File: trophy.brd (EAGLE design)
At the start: 75.9 x 26.7 mm, 20 parts, among them J1 AVR_SPI_PROG_3X2PTH, U1 ATTINY85SOIC8

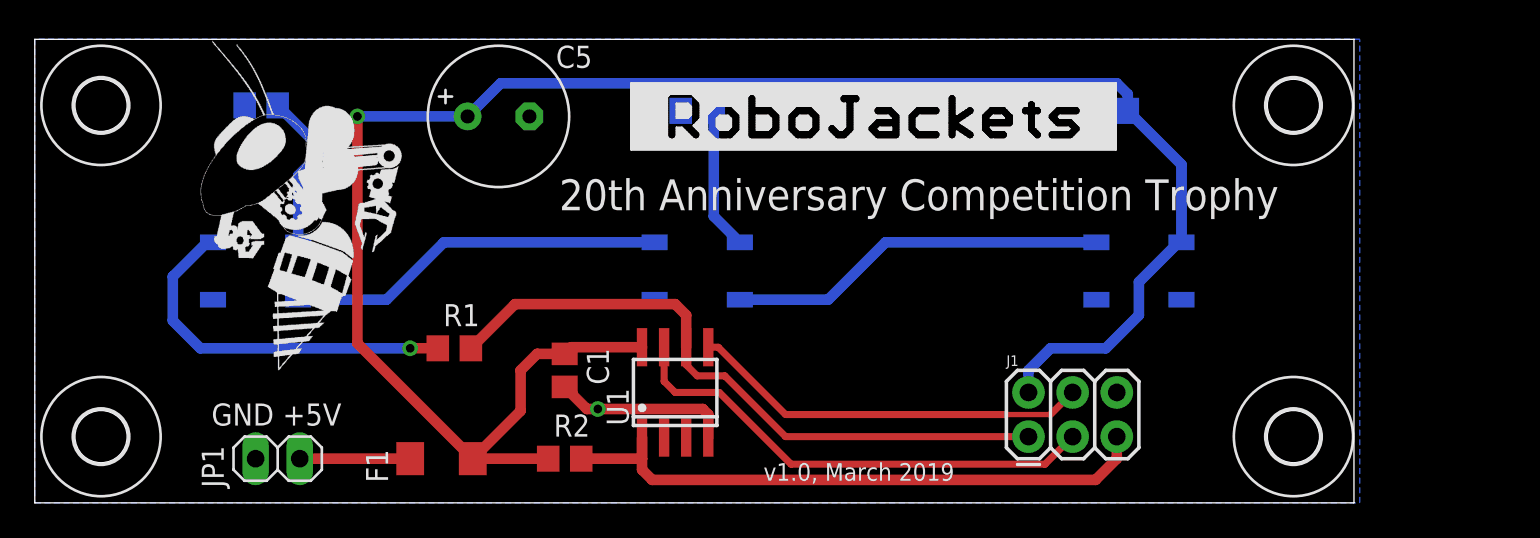
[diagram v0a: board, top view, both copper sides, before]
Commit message: Round corners and make final tweaks for trophy
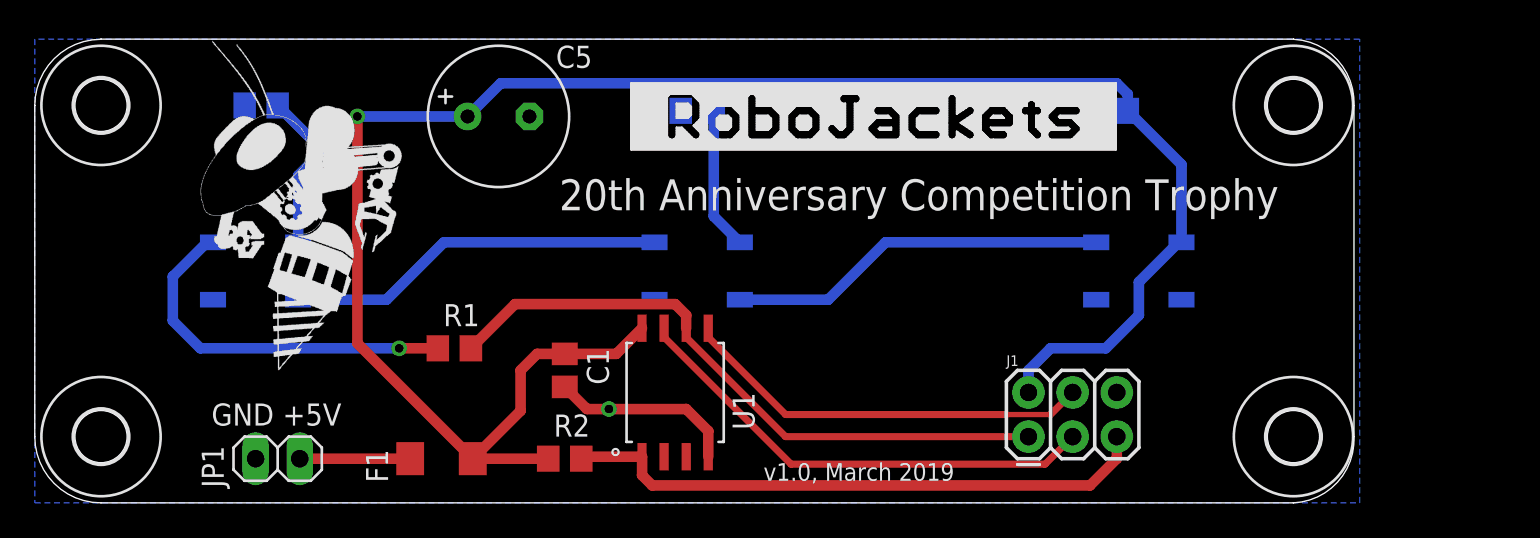
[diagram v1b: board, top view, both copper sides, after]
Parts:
- U1: value ATTINY85SOIC8 -> ATTINY85; device JoshCustom:SOIC8 -> JoshCustom:8S2
- turned U1 to 90 degrees
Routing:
- net MISO: track 38.0 -> 37.0 mm
- net MOSI: track 23.1 -> 23.8 mm
- net !RESET!: track 34.7 -> 34.1 mm
- net GND: track 10.2 -> 10.8 mm
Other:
- outline, holes or cut-outs redrawn
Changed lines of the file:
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@@
 <layer number="49" name="Reference" color="7" fill="1" visible="yes" active="yes"/>
 <layer number="50" name="dxf" color="7" fill="1" visible="no" active="no"/>
-<layer number="51" name="tDocu" color="7" fill="1" visible="yes" active="yes"/>
-<layer number="52" name="bDocu" color="7" fill="1" visible="yes" active="yes"/>
+<layer number="51" name="tDocu" color="7" fill="1" visible="no" active="yes"/>
+<layer number="52" name="bDocu" color="7" fill="1" visible="no" active="yes"/>
 <layer number="53" name="tGND_GNDA" color="7" fill="9" visible="no" active="no"/>
 <layer number="54" name="bGND_GNDA" color="1" fill="9" visible="no" active="no"/>
@@
 <board>
 <plain>
-<wire x1="0" y1="0" x2="75.87" y2="0" width="0" layer="20"/>
-<wire x1="75.87" y1="0" x2="75.87" y2="26.66" width="0" layer="20"/>
-<wire x1="75.87" y1="26.66" x2="0" y2="26.66" width="0" layer="20"/>
-<wire x1="0" y1="26.66" x2="0" y2="0" width="0" layer="20"/>
+<wire x1="3.81" y1="0" x2="72.39" y2="0" width="0" layer="20"/>
+<wire x1="72.39" y1="0" x2="75.87" y2="3.81" width="0" layer="20" curve="90"/>
+<wire x1="75.87" y1="3.81" x2="75.87" y2="22.85" width="0" layer="20"/>
+<wire x1="75.87" y1="22.85" x2="72.4" y2="26.66" width="0" layer="20" curve="90"/>
+<wire x1="72.4" y1="26.66" x2="72.39" y2="26.67" width="0" layer="20"/>
+<wire x1="72.39" y1="26.67" x2="3.81" y2="26.67" width="0" layer="20"/>
+<wire x1="3.81" y1="26.67" x2="3.8" y2="26.66" width="0" layer="20"/>
+<wire x1="3.8" y1="26.66" x2="0" y2="22.85" width="0" layer="20" curve="90"/>
+<wire x1="0" y1="22.85" x2="0" y2="22.86" width="0" layer="20"/>
+<wire x1="0" y1="22.85" x2="0" y2="3.81" width="0" layer="20"/>
+<wire x1="0" y1="3.81" x2="3.81" y2="0" width="0" layer="20" curve="90"/>
 <text x="10.16" y="4.445" size="1.27" layer="21">GND +5V</text>
-<text x="30.1625" y="16.8275" size="1.778" layer="21">20th Anniversary Competition Trophy</text>
-<text x="41.91" y="1.27" size="1.016" layer="21">v1.0, March 2019</text>
+<text x="30.1625" y="16.8275" size="1.778" layer="21" font="vector">20th Anniversary Competition Trophy</text>
+<text x="41.91" y="1.27" size="1.016" layer="21" font="vector" ratio="7">v1.0, March 2019</text>
 </plain>
 <attributes>
@@
 <attribute name="NAME" x="29.845" y="3.81" size="1.27" layer="25" ratio="7"/>
 </element>
-<element name="U1" library="JoshCustom" package="SOIC8" value="ATTINY85SOIC8" x="36.83" y="6.35" smashed="yes">
-<attribute name="NAME" x="34.163" y="4.445" size="1.27" layer="25" font="vector" ratio="7" rot="R90"/>
+<element name="U1" library="JoshCustom" package="8S2" value="ATTINY85" x="36.83" y="6.35" smashed="yes" rot="R90">
+<attribute name="NAME" x="40.132" y="6.35" size="1.27" layer="25" font="vector" ratio="7" rot="R270"/>
 </element>
 <element name="U$1" library="holes" library_urn="urn:adsk.eagle:library:237" package="3,0" package3d_urn="urn:adsk.eagle:package:14277/1" value="" x="3.81" y="3.81" smashed="yes"/>
@@
 <wire x1="27.94" y1="7.62" x2="28.89" y2="8.57" width="0.6096" layer="1"/>
 <wire x1="28.89" y1="8.57" x2="30.48" y2="8.57" width="0.6096" layer="1"/>
-<wire x1="30.48" y1="8.57" x2="30.86" y2="8.95" width="0.6096" layer="1"/>
-<wire x1="30.86" y1="8.95" x2="34.925" y2="8.95" width="0.6096" layer="1"/>
 <wire x1="24.892" y1="22.225" x2="18.555" y2="22.225" width="0.6096" layer="16"/>
 <wire x1="18.555" y1="22.225" x2="16.57875" y2="20.24875" width="0.6096" layer="16"/>
@@
 <wire x1="63.5" y1="12.7" x2="65.785" y2="14.985" width="0.6096" layer="16"/>
 <wire x1="65.785" y1="14.985" x2="65.95" y2="14.985" width="0.6096" layer="16"/>
+<wire x1="30.48" y1="8.57" x2="33.4493" y2="8.57" width="0.6096" layer="1"/>
+<wire x1="34.925" y1="10.0457" x2="33.4493" y2="8.57" width="0.6096" layer="1"/>
 </signal>
 <signal name="GND">
@@
 </polygon>
 <wire x1="30.48" y1="6.67" x2="31.7525" y2="5.3975" width="0.6096" layer="1"/>
-<wire x1="38.4175" y1="5.3975" x2="38.735" y2="5.08" width="0.6096" layer="1"/>
-<wire x1="38.735" y1="5.08" x2="38.735" y2="3.75" width="0.6096" layer="1"/>
-<wire x1="31.7525" y1="5.3975" x2="32.385" y2="5.3975" width="0.6096" layer="1"/>
-<wire x1="32.385" y1="5.3975" x2="38.4175" y2="5.3975" width="0.6096" layer="1"/>
-<via x="32.385" y="5.3975" extent="1-16" drill="0.5"/>
+<wire x1="31.7525" y1="5.3975" x2="33.02" y2="5.3975" width="0.6096" layer="1"/>
+<via x="33.02" y="5.3975" extent="1-16" drill="0.5"/>
+<wire x1="37.465" y1="5.3975" x2="38.735" y2="4.1275" width="0.6096" layer="1"/>
+<wire x1="37.465" y1="5.3975" x2="33.02" y2="5.3975" width="0.6096" layer="1"/>
+<wire x1="38.735" y1="4.1275" x2="38.735" y2="2.6543" width="0.6096" layer="1"/>
 </signal>
 <signal name="N$1">
@@
 <contactref element="R2" pad="2"/>
 <contactref element="J1" pad="5"/>
-<wire x1="34.925" y1="3.75" x2="34.925" y2="2.54" width="0.6096" layer="1"/>
-<wire x1="34.925" y1="2.54" x2="34.925" y2="1.905" width="0.6096" layer="1"/>
-<wire x1="34.925" y1="1.905" x2="35.5092" y2="1.3208" width="0.6096" layer="1"/>
-<wire x1="61.0108" y1="1.3208" x2="62.23" y2="2.54" width="0.6096" layer="1"/>
+<wire x1="35.5092" y1="1.0033" x2="34.925" y2="1.5875" width="0.6096" layer="1"/>
+<wire x1="60.6933" y1="1.0033" x2="62.23" y2="2.54" width="0.6096" layer="1"/>
 <wire x1="62.23" y1="2.54" x2="62.23" y2="3.81" width="0.6096" layer="1"/>
-<wire x1="35.5092" y1="1.3208" x2="61.0108" y2="1.3208" width="0.6096" layer="1"/>
-<wire x1="31.43" y1="2.54" x2="34.925" y2="2.54" width="0.6096" layer="1"/>
+<wire x1="35.5092" y1="1.0033" x2="60.6933" y2="1.0033" width="0.6096" layer="1"/>
+<wire x1="31.43" y1="2.54" x2="31.5443" y2="2.6543" width="0.6096" layer="1"/>
+<wire x1="31.5443" y1="2.6543" x2="34.925" y2="2.6543" width="0.6096" layer="1"/>
+<wire x1="34.925" y1="1.5875" x2="34.925" y2="2.6543" width="0.6096" layer="1"/>
 </signal>
 <signal name="SCK">
 <contactref element="U1" pad="7"/>
 <contactref element="J1" pad="3"/>
-<wire x1="36.195" y1="8.95" x2="36.195" y2="6.985" width="0.4064" layer="1"/>
-<wire x1="36.195" y1="6.985" x2="36.83" y2="6.35" width="0.4064" layer="1"/>
-<wire x1="36.83" y1="6.35" x2="39.37" y2="6.35" width="0.4064" layer="1"/>
-<wire x1="39.37" y1="6.35" x2="43.4975" y2="2.2225" width="0.4064" layer="1"/>
-<wire x1="43.4975" y1="2.2225" x2="58.1025" y2="2.2225" width="0.4064" layer="1"/>
-<wire x1="58.1025" y1="2.2225" x2="59.69" y2="3.81" width="0.4064" layer="1"/>
+<wire x1="59.69" y1="3.81" x2="58.1025" y2="2.2225" width="0.4064" layer="1"/>
+<wire x1="58.1025" y1="2.2225" x2="43.4975" y2="2.2225" width="0.4064" layer="1"/>
+<wire x1="36.195" y1="9.525" x2="43.4975" y2="2.2225" width="0.4064" layer="1"/>
+<wire x1="36.195" y1="10.0457" x2="36.195" y2="9.525" width="0.4064" layer="1"/>
 </signal>
 <signal name="MISO">
@@
 <contactref element="J1" pad="1"/>
 <contactref element="R1" pad="2"/>
-<wire x1="37.465" y1="8.95" x2="37.465" y2="10.795" width="0.6096" layer="1"/>
 <wire x1="37.465" y1="10.795" x2="36.83" y2="11.43" width="0.6096" layer="1"/>
-<wire x1="37.465" y1="8.95" x2="37.465" y2="7.9375" width="0.4064" layer="1"/>
-<wire x1="37.465" y1="7.9375" x2="38.1" y2="7.3025" width="0.4064" layer="1"/>
-<wire x1="38.1" y1="7.3025" x2="39.6875" y2="7.3025" width="0.4064" layer="1"/>
-<wire x1="39.6875" y1="7.3025" x2="43.18" y2="3.81" width="0.4064" layer="1"/>
-<wire x1="43.18" y1="3.81" x2="57.15" y2="3.81" width="0.4064" layer="1"/>
+<wire x1="57.15" y1="3.81" x2="43.18" y2="3.81" width="0.4064" layer="1"/>
 <wire x1="36.83" y1="11.43" x2="27.62" y2="11.43" width="0.6096" layer="1"/>
 <wire x1="27.62" y1="11.43" x2="25.08" y2="8.89" width="0.6096" layer="1"/>
+<wire x1="43.18" y1="3.81" x2="37.465" y2="9.525" width="0.4064" layer="1"/>
+<wire x1="37.465" y1="9.525" x2="37.465" y2="10.0457" width="0.4064" layer="1"/>
+<wire x1="37.465" y1="10.0457" x2="37.465" y2="10.795" width="0.6096" layer="1"/>
 </signal>
 <signal name="MOSI">
 <contactref element="U1" pad="5"/>
 <contactref element="J1" pad="4"/>
-<wire x1="38.735" y1="8.95" x2="39.31" y2="8.95" width="0.4064" layer="1"/>
-<wire x1="39.31" y1="8.95" x2="43.18" y2="5.08" width="0.4064" layer="1"/>
-<wire x1="43.18" y1="5.08" x2="55.88" y2="5.08" width="0.4064" layer="1"/>
+<wire x1="55.88" y1="5.08" x2="43.18" y2="5.08" width="0.4064" layer="1"/>
 <wire x1="55.88" y1="5.08" x2="58.42" y2="5.08" width="0.3048" layer="1"/>
 <wire x1="58.42" y1="5.08" x2="59.69" y2="6.35" width="0.4064" layer="1"/>
+<wire x1="38.735" y1="9.525" x2="43.18" y2="5.08" width="0.4064" layer="1"/>
+<wire x1="38.735" y1="10.0457" x2="38.735" y2="9.525" width="0.4064" layer="1"/>
 </signal>
 <signal name="N$3">
 <contactref element="JP1" pad="2"/>
 <contactref element="F1" pad="2"/>
-<wire x1="21.59" y1="2.54" x2="15.24" y2="2.54" width="0.6096" layer="1"/>
+<wire x1="15.24" y1="2.54" x2="21.59" y2="2.54" width="0.6096" layer="1"/>
 </signal>
 <signal name="N$6">
 <contactref element="LED1" pad="4"/>
 <contactref element="R1" pad="1"/>
-<wire x1="23.18" y1="8.89" x2="21.59" y2="8.89" width="0.6096" layer="1"/>
-<via x="21.59" y="8.89" extent="1-16" drill="0.5"/>
+<wire x1="23.18" y1="8.89" x2="20.955" y2="8.89" width="0.6096" layer="1"/>
+<via x="20.955" y="8.89" extent="1-16" drill="0.5"/>
 <wire x1="9.525" y1="8.89" x2="7.9375" y2="10.4775" width="0.6096" layer="16"/>
 <wire x1="7.9375" y1="10.4775" x2="7.9375" y2="13.0175" width="0.6096" layer="16"/>
 <wire x1="7.9375" y1="13.0175" x2="9.905" y2="14.985" width="0.6096" layer="16"/>
 <wire x1="9.905" y1="14.985" x2="10.25" y2="14.985" width="0.6096" layer="16"/>
-<wire x1="21.59" y1="8.89" x2="9.525" y2="8.89" width="0.6096" layer="16"/>
+<wire x1="20.955" y1="8.89" x2="9.525" y2="8.89" width="0.6096" layer="16"/>
 </signal>
 </signals>
